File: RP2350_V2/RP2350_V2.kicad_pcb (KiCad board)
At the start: 4 copper layers, 68.9 x 112.1 mm, 148 parts, among them IC1 DMP1045U-7, IC2 DMP1045U-7, IC3 DMP1045U-7, IC4 DMP1045U-7, IC5 DMP1045U-7, IC6 DMP1045U-7, J1 Conn_01x04_Pin, J10 S0991-46R, J2 S0991-46R, J3 USB_C_Receptacle_USB2.0_16P, J4 IPEX1, J5 Conn_01x08_Socket, J6 Conn_01x02_Pin, J7 Conn_01x04_Pin, J8 S0991-46R, J9 S0991-46R, SW1 PTS 647 SN50 SMTR2 LFS, SW10 PTS 647 SN50 SMTR2 LFS, SW11 PTS 647 SN50 SMTR2 LFS, SW12 PTS 647 SN50 SMTR2 LFS, SW13 PTS 647 SN50 SMTR2 LFS, SW14 PTS 647 SN50 SMTR2 LFS, SW4 PTS 647 SN50 SMTR2 LFS, SW9 PTS 647 SN50 SMTR2 LFS, U1 RP2350_60QFN, U2 W25Q128JVS, U3 TPS62811QWRWYRQ1, U4 MCP73812T-420I-OT, U5 TLV3012AIDCKR, U6 74HC14, X1 ABM8-272-T3

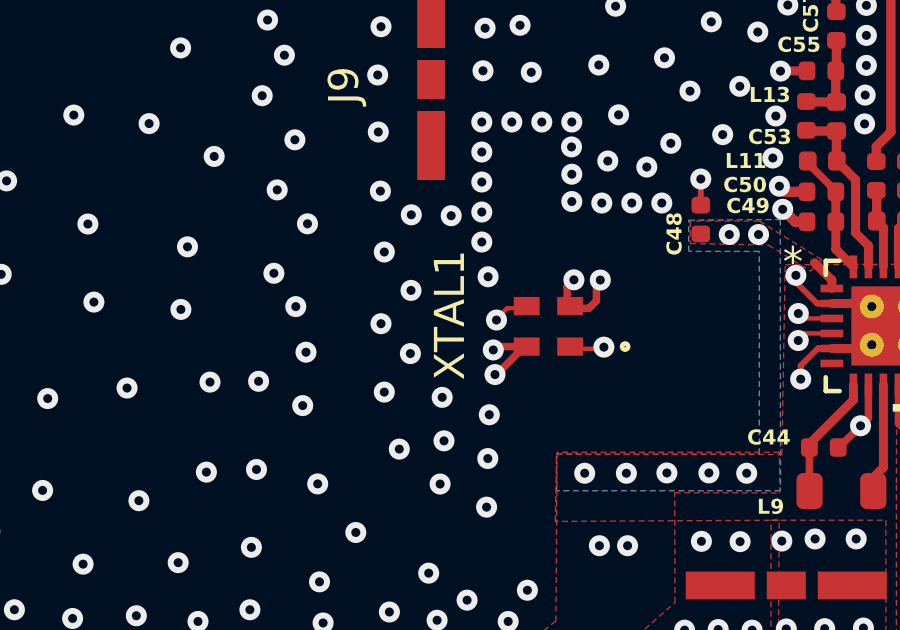
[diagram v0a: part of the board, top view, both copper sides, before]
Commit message: update XTAL1 to X2, regen fab exports
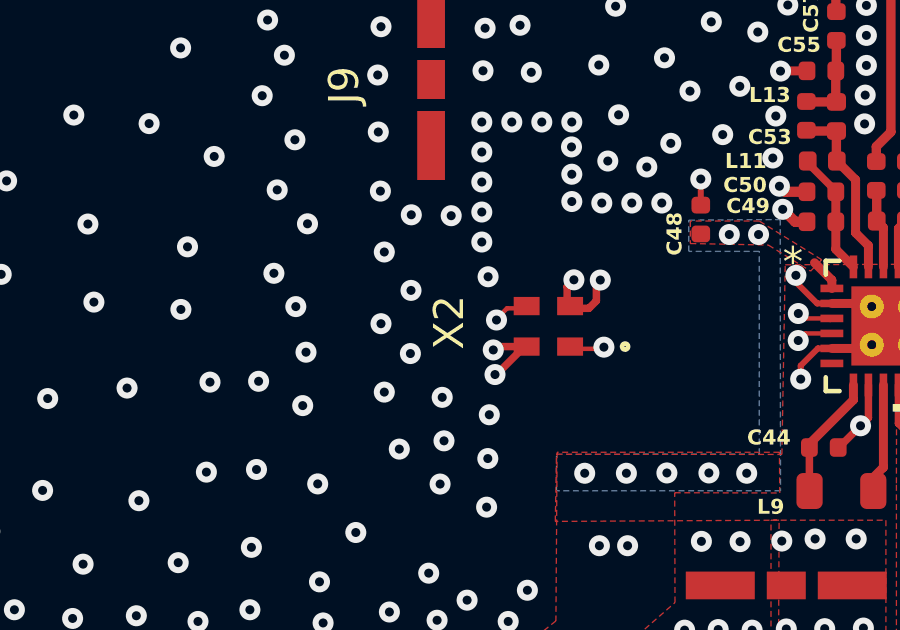
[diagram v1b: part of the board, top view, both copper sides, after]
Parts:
- renumbered XTAL1 to X2
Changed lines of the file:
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@@
 		(at 134.22 72.6325 180)
 		(tags "NX2016SA-32M-EXS00A-CS06465 ")
-		(property "Reference" "XTAL1"
-			(at 3.28 0.377559 90)
+		(property "Reference" "X2"
+			(at 3.31 0.1325 90)
 			(unlocked yes)
 			(layer "F.SilkS")
@@
 					(thickness 0.15)
 				)
+			)
+		)
+		(property "LCSC" "C5137195"
+			(at 0 0 -90)
+			(unlocked yes)
+			(layer "F.Fab")
+			(hide yes)
+			(effects
+				(font
+					(size 1 1)
+					(thickness 0.15)
+				)

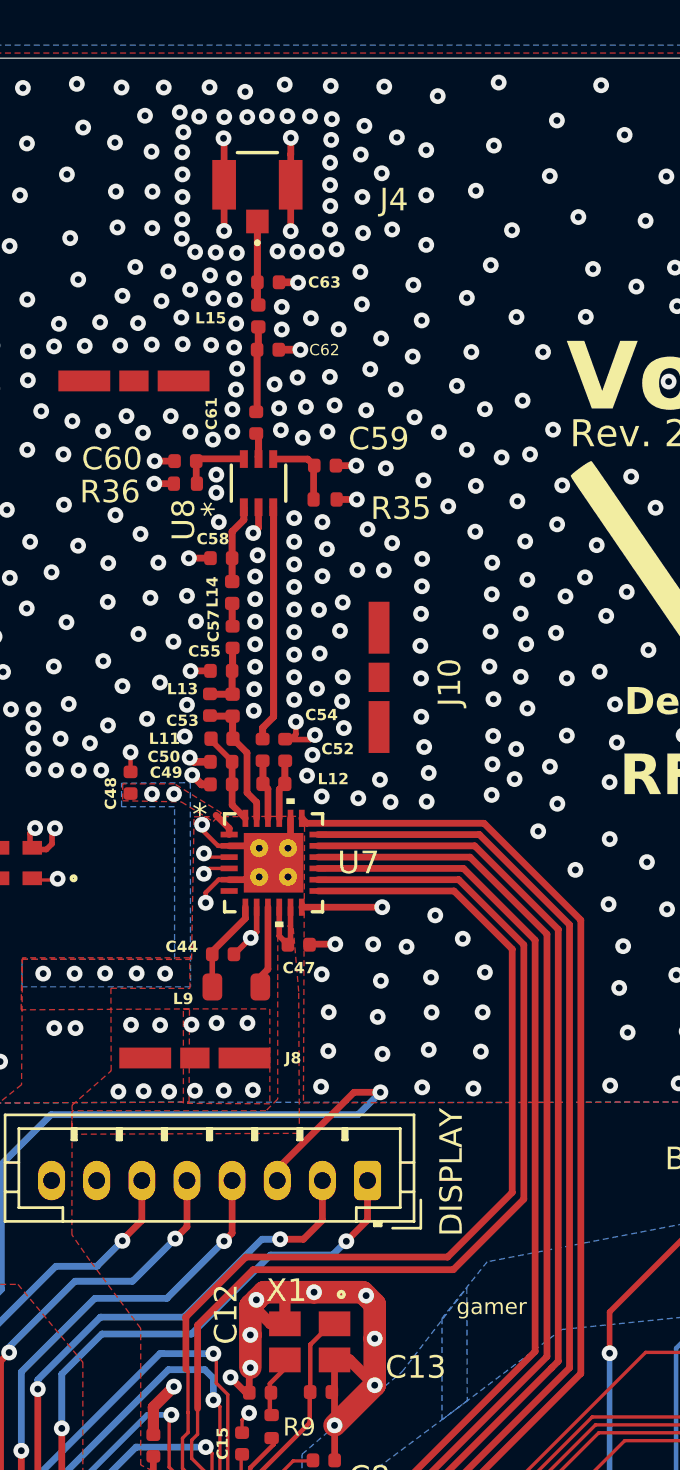
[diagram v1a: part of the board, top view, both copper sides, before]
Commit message: via refinement
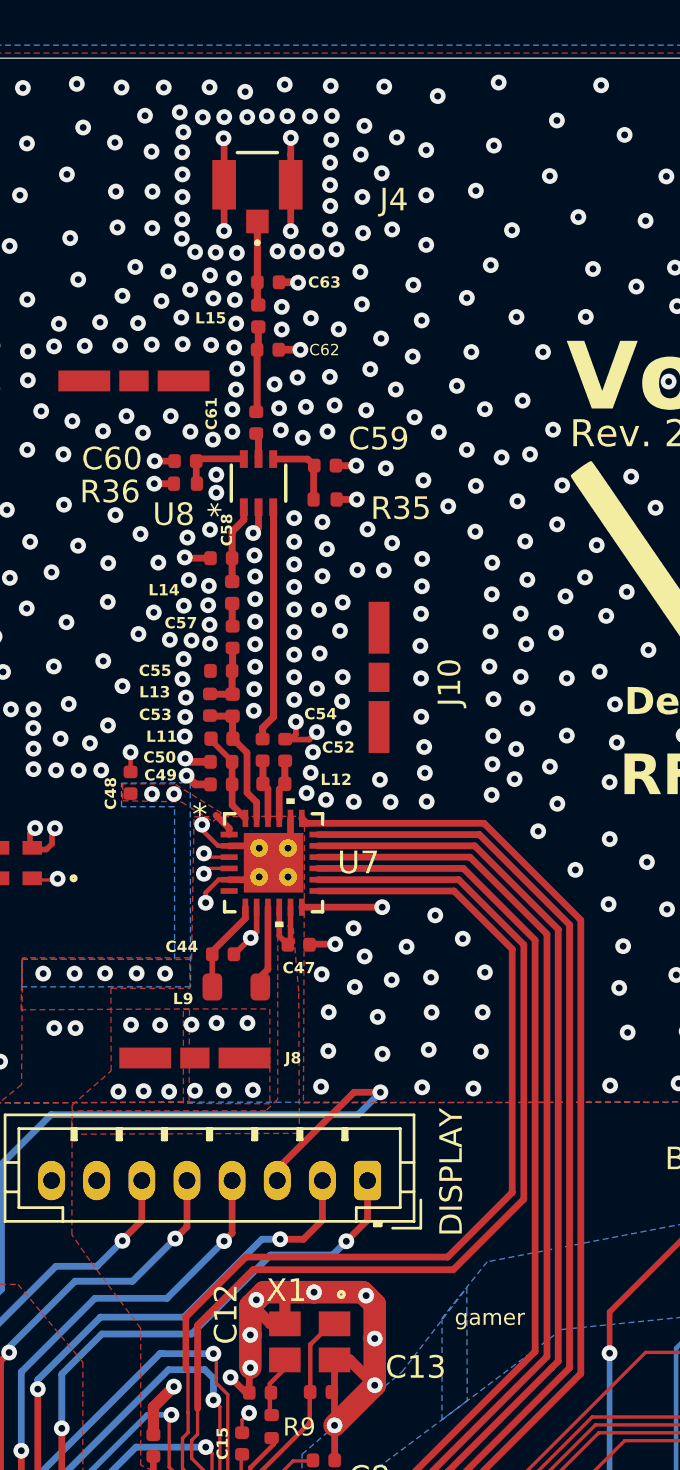
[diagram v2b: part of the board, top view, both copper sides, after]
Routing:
- net GND: track 202.2 -> 202.0 mm, vias 654 -> 663

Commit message: jhsdbdhjsvfdsm
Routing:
- net GND: vias 663 -> 665
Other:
- board text removed: "gamer"

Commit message: rev2.0 tapeout
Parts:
- removed the G*** at (156.4, 126.6)
- added G***: LOGO, LOGO, F.Cu at (118.3, 95.7)
- added G***: LOGO, LOGO, F.Cu at (117.1, 130.5)
- added G***: LOGO, LOGO, F.Cu at (122.0, 56.9)
- added G***: LOGO, LOGO, F.Cu at (156.5, 128.3)
- moved R34 10.3 mm to (161.3, 142.4), turned to 90 degrees
- moved IC3 7.94 mm to (158.8, 142.8), turned to -90 degrees
- moved R38 7.58 mm to (122.1, 106.9)
- moved D6 5.55 mm to (119.4, 107.2), turned to 0 degrees
- moved SW10 1.30 mm to (123.8, 131.5)
- moved SW14 1.30 mm to (123.8, 111.5)
- moved SW9 1.30 mm to (123.8, 121.5)
- moved IC4 0.86 mm to (119.8, 104.5), turned to 0 degrees
- moved SW1 0.55 mm to (119.8, 85.9)
- moved R1 0.49 mm to (128.4, 87.5)
- moved R37 0.35 mm to (122.2, 105.3), turned to 90 degrees
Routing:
- net /UVLO_RST: track 37.7 -> 51.9 mm
- net +3V3: track 183.6 -> 176.6 mm
- net Net-(IC4-G): track 1.44 -> 4.49 mm
- net Net-(IC3-S): track 1.81 -> 4.25 mm
- net GND: track 202.0 -> 200.7 mm, vias 665 -> 675
- net Net-(R20-Pad2): track 70.9 -> 69.6 mm
- net Net-(R23-Pad2): track 65.0 -> 63.8 mm
- net /RUN_IN: track 9.96 -> 10.9 mm
- net Net-(R24-Pad2): track 75.7 -> 75.1 mm
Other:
- board text added: "DON'T PANIC DON'T PANIC DON'T PANIC"
